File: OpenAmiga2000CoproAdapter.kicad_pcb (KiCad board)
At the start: 2 copper layers, 112 x 37.5 mm, 18 parts, among them CN1 A2000_COPRO_SLOT, P1 CONN_2, P10 CONN_1, P11 CONN_1, P12 CONN_1, P13 CONN_1, P14 CONN_1, P15 CONN_1, P2 CONN_2, P3 CONN_2, P4 CONN_2, P5 CONN_1, P6 CONN_1, P7 CONN_1, P8 CONN_1, P9 CONN_1, P99 OSHW_LOGO, U1 68000D

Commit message: More minor cosmetic fixes
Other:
- board text added: "~INT2"
- board text added: "~OVR"
- board text removed: "INT2"
- board text removed: "OVR"
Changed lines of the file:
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@@
     (add_net GND)
+  )
+  (module OpenAmiga2000CoproAdapter:PinHeader_1x02_P2.54mm_Vertical (layer B.Cu)
+    (at 116.078 123.3805 90)
+    (descr "Through hole straight pin header, 1x02, 2.54mm pitch, single row")
+    (tags "Through hole pin header THT 1x02 2.54mm single row")
+    (fp_text reference P1 (at 0 2.33 90) (layer B.SilkS) hide
+      (effects (font (size 1 1) (thickness 0.15)) (justify mirror))
+    )
+    (fp_text value CONN_2 (at 0 -4.87 90) (layer B.Fab)
+      (effects (font (size 1 1) (thickness 0.15)) (justify mirror))
+    )
+    (fp_line (start -0.635 1.27) (end 1.27 1.27) (layer B.Fab) (width 0.1))
+    (fp_line (start 1.27 1.27) (end 1.27 -3.81) (layer B.Fab) (width 0.1))
+    (fp_line (start 1.27 -3.81) (end -1.27 -3.81) (layer B.Fab) (width 0.1))
+    (fp_line (start -1.27 -3.81) (end -1.27 0.635) (layer B.Fab) (width 0.1))
+    (fp_line (start -1.27 0.635) (end -0.635 1.27) (layer B.Fab) (width 0.1))
+    (fp_line (start -1.27 -3.937) (end 1.27 -3.937) (layer B.SilkS) (width 0.12))
+    (fp_line (start -1.27 1.397) (end -1.27 -3.937) (layer B.SilkS) (width 0.12))
+    (fp_line (start 1.27 1.397) (end 1.27 -3.937) (layer B.SilkS) (width 0.12))
+    (fp_line (start -1.27 1.397) (end 1.27 1.397) (layer B.SilkS) (width 0.12))
+    (fp_line (start -1.8 1.8) (end -1.8 -4.35) (layer B.CrtYd) (width 0.05))
+    (fp_line (start -1.8 -4.35) (end 1.8 -4.35) (layer B.CrtYd) (width 0.05))
+    (fp_line (start 1.8 -4.35) (end 1.8 1.8) (layer B.CrtYd) (width 0.05))
+    (fp_line (start 1.8 1.8) (end -1.8 1.8) (layer B.CrtYd) (width 0.05))
+    (fp_text user %R (at 0 -1.27) (layer B.Fab)
+      (effects (font (size 1 1) (thickness 0.15)) (justify mirror))
+    )
+    (pad 1 thru_hole circle (at 0 0 90) (size 1.7 1.7) (drill 1) (layers *.Cu *.Mask)
+      (net 5 "Net-(CN1-Pad19)"))
+    (pad 2 thru_hole oval (at 0 -2.54 90) (size 1.7 1.7) (drill 1) (layers *.Cu *.Mask)
+      (net 4 "Net-(CN1-Pad17)"))
+    (model ${KISYS3DMOD}/Connector_PinHeader_2.54mm.3dshapes/PinHeader_1x02_P2.54mm_Vertical.wrl
+      (at (xyz 0 0 0))
+      (scale (xyz 1 1 1))
+      (rotate (xyz 0 0 0))
+    )
   )
   (module OpenAmiga2000CoproAdapter:A2000_COPRO_SLOT (layer F.Cu)
@@
            (xy 0 0.75) (xy -0.5 0.75) (xy -0.5 -0.75) (xy 0 -0.75)) (width 0))
       ))
-  )
-  (module OpenAmiga2000CoproAdapter:PinHeader_1x02_P2.54mm_Vertical (layer B.Cu)
-    (at 116.078 123.3805 90)
-    (descr "Through hole straight pin header, 1x02, 2.54mm pitch, single row")
-    (tags "Through hole pin header THT 1x02 2.54mm single row")
-    (fp_text reference P1 (at 0 2.33 90) (layer B.SilkS) hide
-      (effects (font (size 1 1) (thickness 0.15)) (justify mirror))
-    )
-    (fp_text value CONN_2 (at 0 -4.87 90) (layer B.Fab)
-      (effects (font (size 1 1) (thickness 0.15)) (justify mirror))
-    )
-    (fp_line (start -0.635 1.27) (end 1.27 1.27) (layer B.Fab) (width 0.1))
-    (fp_line (start 1.27 1.27) (end 1.27 -3.81) (layer B.Fab) (width 0.1))
-    (fp_line (start 1.27 -3.81) (end -1.27 -3.81) (layer B.Fab) (width 0.1))
-    (fp_line (start -1.27 -3.81) (end -1.27 0.635) (layer B.Fab) (width 0.1))
-    (fp_line (start -1.27 0.635) (end -0.635 1.27) (layer B.Fab) (width 0.1))
-    (fp_line (start -1.27 -3.81) (end 1.27 -3.81) (layer B.SilkS) (width 0.12))
-    (fp_line (start -1.27 1.397) (end -1.27 -3.81) (layer B.SilkS) (width 0.12))
-    (fp_line (start 1.27 1.397) (end 1.27 -3.81) (layer B.SilkS) (width 0.12))
-    (fp_line (start -1.27 1.397) (end 1.27 1.397) (layer B.SilkS) (width 0.12))
-    (fp_line (start -1.8 1.8) (end -1.8 -4.35) (layer B.CrtYd) (width 0.05))
-    (fp_line (start -1.8 -4.35) (end 1.8 -4.35) (layer B.CrtYd) (width 0.05))
-    (fp_line (start 1.8 -4.35) (end 1.8 1.8) (layer B.CrtYd) (width 0.05))
-    (fp_line (start 1.8 1.8) (end -1.8 1.8) (layer B.CrtYd) (width 0.05))
-    (fp_text user %R (at 0 -1.27) (layer B.Fab)
-      (effects (font (size 1 1) (thickness 0.15)) (justify mirror))
-    )
-    (pad 1 thru_hole circle (at 0 0 90) (size 1.7 1.7) (drill 1) (layers *.Cu *.Mask)
-      (net 5 "Net-(CN1-Pad19)"))
-    (pad 2 thru_hole oval (at 0 -2.54 90) (size 1.7 1.7) (drill 1) (layers *.Cu *.Mask)
-      (net 4 "Net-(CN1-Pad17)"))
-    (model ${KISYS3DMOD}/Connector_PinHeader_2.54mm.3dshapes/PinHeader_1x02_P2.54mm_Vertical.wrl
-      (at (xyz 0 0 0))
-      (scale (xyz 1 1 1))
-      (rotate (xyz 0 0 0))
-    )
   )
   (module Symbol:OSHW-Logo_7.5x8mm_Copper (layer B.Cu)
@@
     (effects (font (size 1 1) (thickness 0.2)) (justify mirror))
   )
-  (gr_text INT2 (at 118.618 123.3805 90) (layer B.SilkS)
-    (effects (font (size 1 1) (thickness 0.2)) (justify mirror))
-  )
-  (gr_text OVR (at 110.998 123.3805 90) (layer B.SilkS)
-    (effects (font (size 1 1) (thickness 0.2)) (justify mirror))
-  )
+  (gr_text ~INT2 (at 118.872 123.3805 90) (layer B.SilkS)
+    (effects (font (size 1 1) (thickness 0.2)) (justify mirror))
+  )
+  (gr_text ~OVR (at 111.252 123.3805 90) (layer B.SilkS)
+    (effects (font (size 1 1) (thickness 0.2)) (justify mirror))
+  )

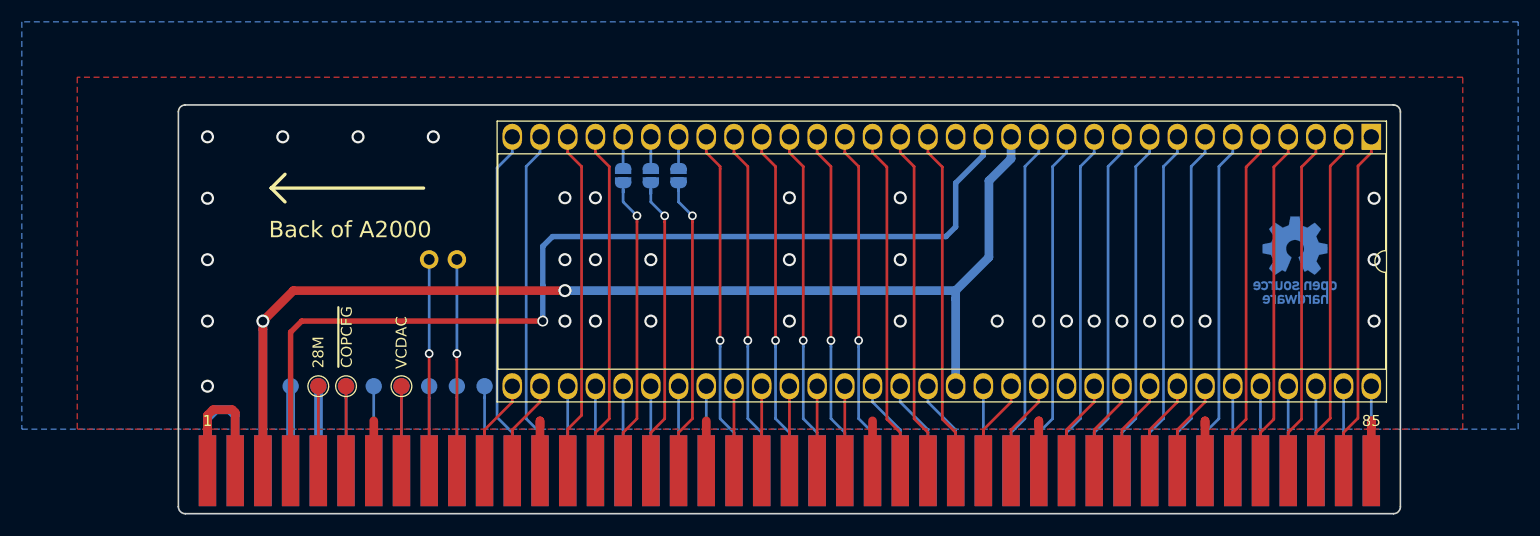
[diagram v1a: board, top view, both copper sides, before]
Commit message: Make board ~0.4mm narrower for a better fit
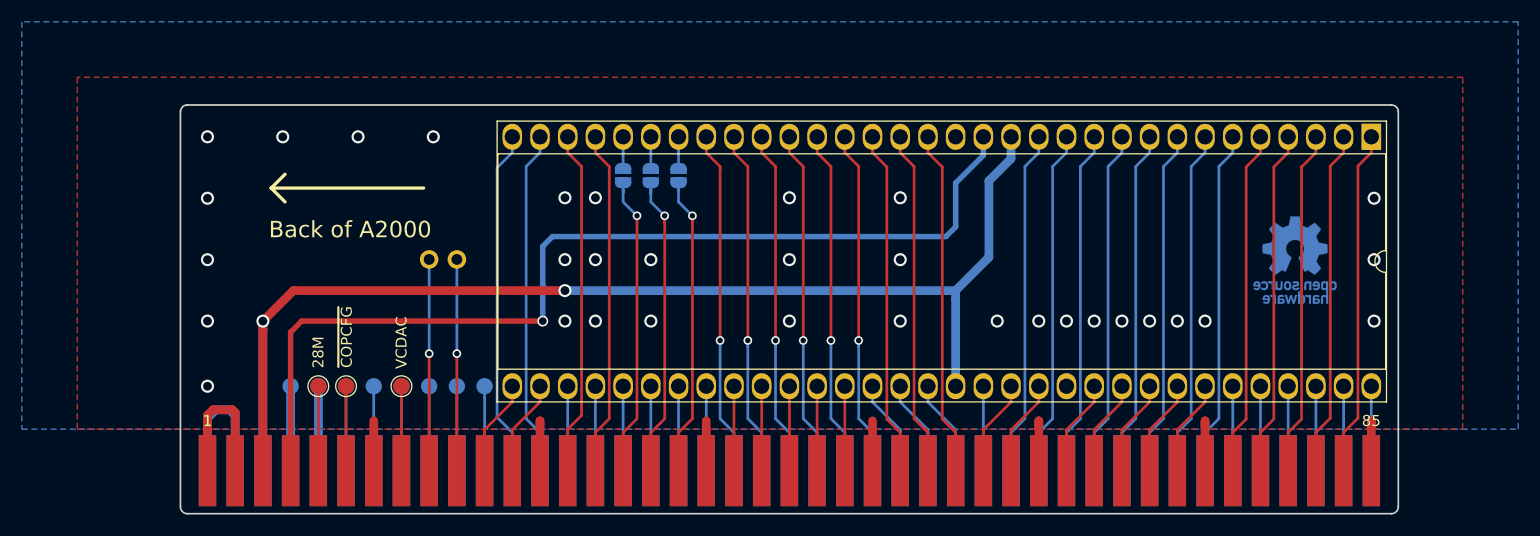
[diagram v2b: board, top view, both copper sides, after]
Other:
- board size 112 x 37.5 mm -> 111.6 x 37.5 mm
- board text added: "V3"
- board text removed: "V2"
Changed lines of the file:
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@@
   (title_block
     (title OpenAmiga2000CoproAdapter)
-    (date 2019-02-14)
-    (rev 2git)
+    (date 2019-03-21)
+    (rev 3)
     (company SukkoPera)
     (comment 1 "Based on work by Kipper2K")
@@
     (44 Edge.Cuts user)
     (45 Margin user hide)
-    (46 B.CrtYd user hide)
-    (47 F.CrtYd user hide)
+    (46 B.CrtYd user)
+    (47 F.CrtYd user)
     (49 F.Fab user hide)
   )
@@
     (pad_to_mask_clearance 0)
     (solder_mask_min_width 0.25)
-    (aux_axis_origin 90.551 146.685)
+    (aux_axis_origin 90.7415 146.685)
+    (grid_origin 90.7415 146.685)
     (visible_elements FFFFFF7F)
     (pcbplotparams
@@
     (effects (font (size 1 1) (thickness 0.2)) (justify right mirror))
   )
-  (gr_text V2 (at 92.075 110.49) (layer B.SilkS)
+  (gr_text V3 (at 92.075 110.49) (layer B.SilkS)
     (effects (font (size 1 1) (thickness 0.2)) (justify mirror))
   )
@@
     (effects (font (size 1 1) (thickness 0.2)) (justify mirror))
   )
-  (gr_arc (start 91.186 109.855) (end 91.186 109.22) (angle -90) (layer Edge.Cuts) (width 0.15))
-  (gr_arc (start 201.93 109.855) (end 202.565 109.855) (angle -90) (layer Edge.Cuts) (width 0.15))
+  (gr_arc (start 91.3765 109.855) (end 91.3765 109.22) (angle -90) (layer Edge.Cuts) (width 0.15))
+  (gr_arc (start 201.7395 109.855) (end 202.3745 109.855) (angle -90) (layer Edge.Cuts) (width 0.15))
   (dimension 37.465 (width 0.3) (layer F.CrtYd)
     (gr_text "37,465 mm" (at 214.271741 127.9525 90) (layer F.CrtYd)
@@
     (arrow2b (pts (xy 212.171741 146.685) (xy 211.58532 145.558496)))
   )
-  (dimension 112.014 (width 0.3) (layer F.CrtYd)
-    (gr_text "112,014 mm" (at 146.558 154.5) (layer F.CrtYd)
+  (dimension 111.633 (width 0.3) (layer F.CrtYd)
+    (gr_text "111,633 mm" (at 146.558 154.5) (layer F.CrtYd)
       (effects (font (size 1.5 1.5) (thickness 0.3)))
     )
-    (feature1 (pts (xy 202.565 146.685) (xy 202.565 152.986421)))
-    (feature2 (pts (xy 90.551 146.685) (xy 90.551 152.986421)))
-    (crossbar (pts (xy 90.551 152.4) (xy 202.565 152.4)))
-    (arrow1a (pts (xy 202.565 152.4) (xy 201.438496 152.986421)))
-    (arrow1b (pts (xy 202.565 152.4) (xy 201.438496 151.813579)))
-    (arrow2a (pts (xy 90.551 152.4) (xy 91.677504 152.986421)))
-    (arrow2b (pts (xy 90.551 152.4) (xy 91.677504 151.813579)))
-  )
-  (gr_arc (start 91.186 146.05) (end 90.551 146.05) (angle -90) (layer Edge.Cuts) (width 0.15))
-  (gr_arc (start 201.93 146.05) (end 201.93 146.685) (angle -90) (layer Edge.Cuts) (width 0.15))
-  (gr_line (start 91.186 146.685) (end 201.93 146.685) (layer Edge.Cuts) (width 0.15))
-  (gr_line (start 90.551 109.855) (end 90.551 146.05) (layer Edge.Cuts) (width 0.15))
-  (gr_line (start 201.93 109.22) (end 91.186 109.22) (layer Edge.Cuts) (width 0.15))
-  (gr_line (start 202.565 146.05) (end 202.565 109.855) (layer Edge.Cuts) (width 0.15))
+    (feature1 (pts (xy 202.3745 146.685) (xy 202.3745 152.986421)))
+    (feature2 (pts (xy 90.7415 146.685) (xy 90.7415 152.986421)))
+    (crossbar (pts (xy 90.7415 152.4) (xy 202.3745 152.4)))
+    (arrow1a (pts (xy 202.3745 152.4) (xy 201.247996 152.986421)))
+    (arrow1b (pts (xy 202.3745 152.4) (xy 201.247996 151.813579)))
+    (arrow2a (pts (xy 90.7415 152.4) (xy 91.868004 152.986421)))
+    (arrow2b (pts (xy 90.7415 152.4) (xy 91.868004 151.813579)))
+  )
+  (gr_arc (start 91.3765 146.05) (end 90.7415 146.05) (angle -90) (layer Edge.Cuts) (width 0.15))
+  (gr_arc (start 201.7395 146.05) (end 201.7395 146.685) (angle -90) (layer Edge.Cuts) (width 0.15))
+  (gr_line (start 91.3765 146.685) (end 201.7395 146.685) (layer Edge.Cuts) (width 0.15))
+  (gr_line (start 90.7415 109.855) (end 90.7415 146.05) (layer Edge.Cuts) (width 0.15))
+  (gr_line (start 201.7395 109.22) (end 91.3765 109.22) (layer Edge.Cuts) (width 0.15))
+  (gr_line (start 202.3745 146.05) (end 202.3745 109.855) (layer Edge.Cuts) (width 0.15))
   (segment (start 93.218 142.748) (end 93.218 138.698) (width 0.8) (layer F.Cu) (net 1) (status 10))
   (segment (start 93.218 137.668) (end 93.726 137.16) (width 0.8) (layer F.Cu) (net 1))
